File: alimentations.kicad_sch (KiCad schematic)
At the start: 0 parts

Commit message: alimentation v1
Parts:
- added C? (x4): 1 uF, symbol pspice:C
- added IC?: 5v to 3.3v, BGA4C35P2X2_64X64X40, symbol TPS7A0333PYCHR:TPS7A0333PYCHR
- added J?: connecteur batterie, symbol Connector_Generic:Conn_01x02
- added S?: Switch, ESE20C343, symbol ESE-20C343:ESE-20C343
- added U?: 3.3v to 1.8v, DSBGA_3PYCHR_TEX, symbol TPS7A0318PYCHR:TPS7A0318PYCHR
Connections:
- new net: J?.2 (Pin_2), S?.A1 (COM_1)
- new net +1V8: C?.1, U?.A2 (OUT)
- new net +3.3V: C?.1, C?.1, IC?.A2 (OUT), U?.A1 (IN), U?.B1 (EN)
- new net +BATT: C?.1, IC?.A1 (IN), IC?.B1 (EN), J?.1 (Pin_1)
- new net GND: C?.2, C?.2, C?.2, C?.2, IC?.B2 (GND), S?.B1 (NO_1), U?.B2 (GND)

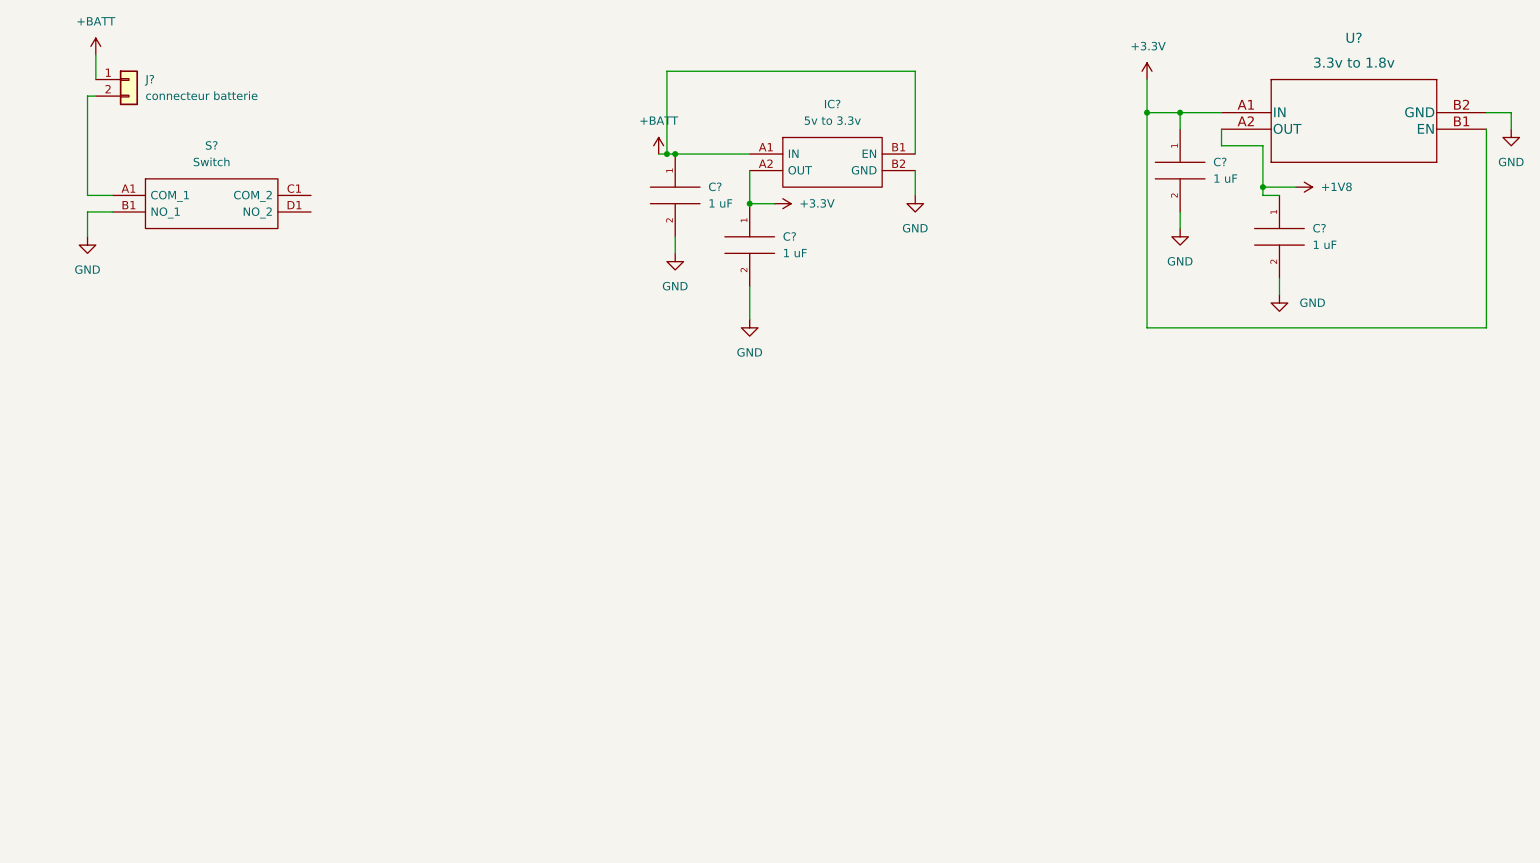
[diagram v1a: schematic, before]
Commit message: Added MAX20077 for 6V output
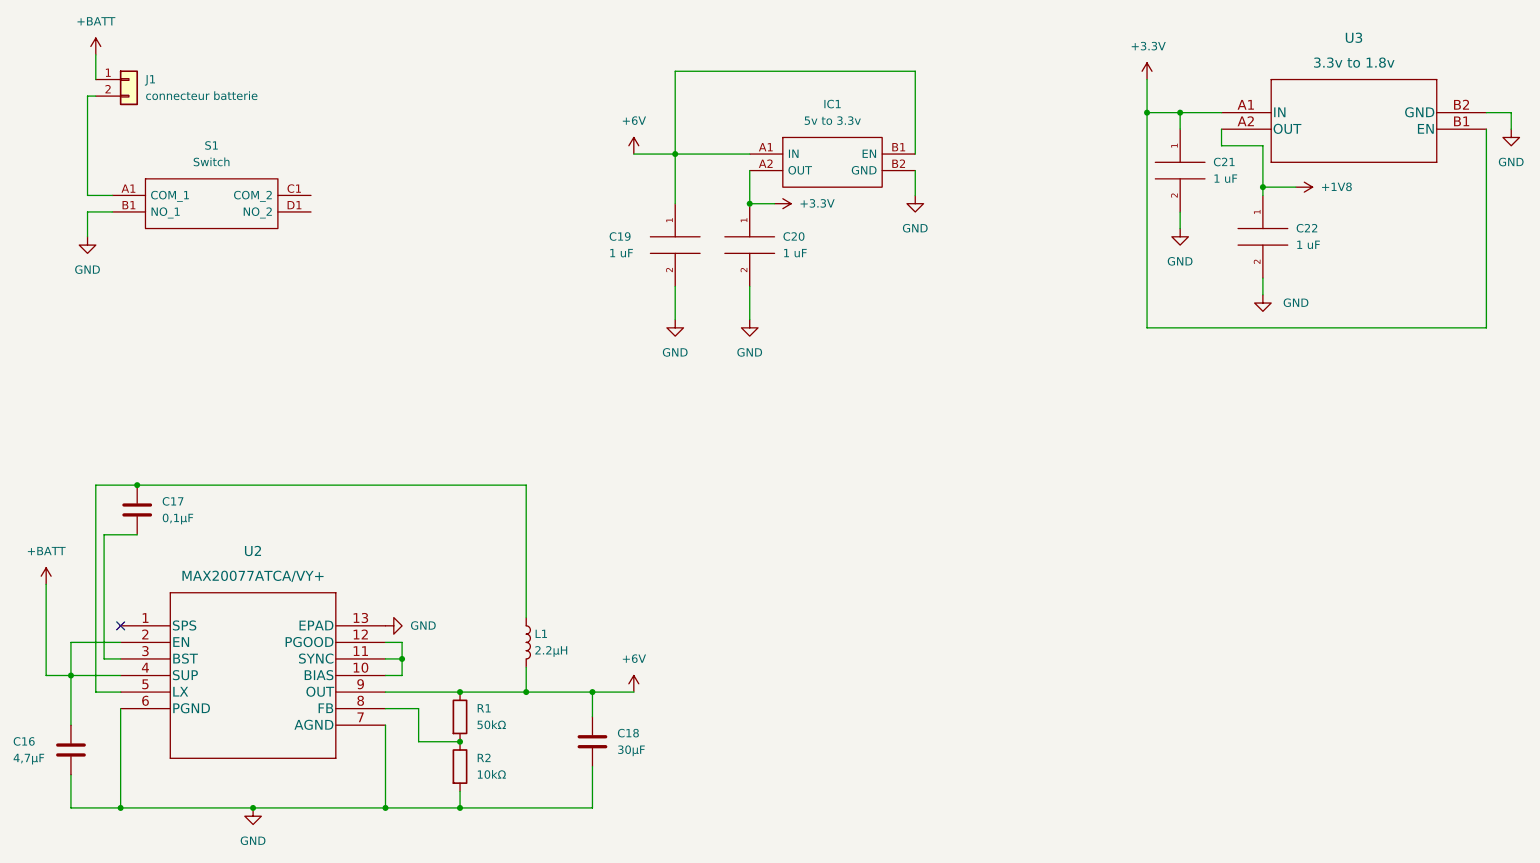
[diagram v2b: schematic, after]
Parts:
- added C16: 4,7µF, symbol Device:C
- added C17: 0,1µF, symbol Device:C
- added C18: 30µF, symbol Device:C
- added L1: 2.2µH, symbol Device:L
- added R1: 50kΩ, symbol Device:R
- added R2: 10kΩ, symbol Device:R
- added U2: MAX20077ATCA/VY+, symbol MAX20077ATCA-VY:MAX20077ATCA/VY+
- IC1: renamed from IC?; footprint BGA4C35P2X2_64X64X40 -> TPS7A0333PYCHR:BGA4C35P2X2_64X64X40
- S1: renamed from S?; footprint ESE20C343 -> ESE-20C343:ESE20C343
- U3: renamed from U?; footprint DSBGA_3PYCHR_TEX -> (none)
- gave numbers to parts that had none: 5
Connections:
- net +BATT: now also C16.1, U2.2 (EN), U2.4 (SUP); no longer C19.1, IC1.A1 (IN), IC1.B1 (EN)
- net GND: now also C16.2, C18.2, R2.2, U2.13 (EPAD), U2.6 (PGND), U2.7 (AGND)
- new net: C17.1, L1.1, U2.5 (LX)
- new net: C17.2, U2.3 (BST)
- new net: R1.2, R2.1, U2.8 (FB)
- new net: U2.10 (BIAS), U2.11 (SYNC), U2.12 (PGOOD)
- new net +6V: C18.1, C19.1, IC1.A1 (IN), IC1.B1 (EN), L1.2, R1.1, U2.9 (OUT)
- no-connect marks 0 -> 1
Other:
- moved on the sheet: C19, C22
